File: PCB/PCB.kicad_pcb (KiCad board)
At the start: 4 copper layers, 54 x 29 mm, 90 parts, among them J1 USB_B_Micro, J2 Conn_01x02, Q1 PJA3428, Q2 PJA3428, Q3 AO3401A, SW1 SW_Push, SW2 SW_Push, SW3 SW_Push, SW4 ON/OFF, U1 ESP32-PICO-MINI-02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

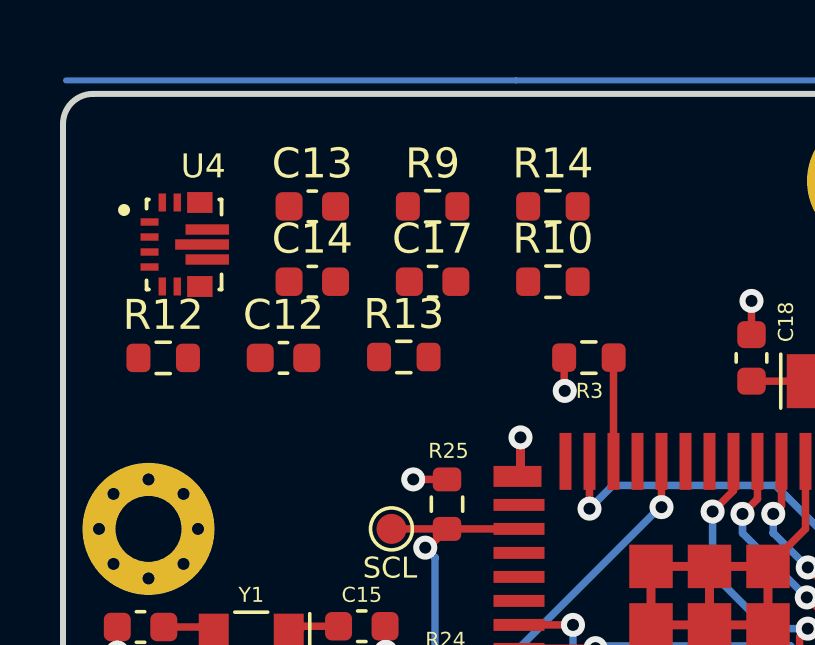
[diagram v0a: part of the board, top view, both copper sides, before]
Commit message: buck-boost pcb changes
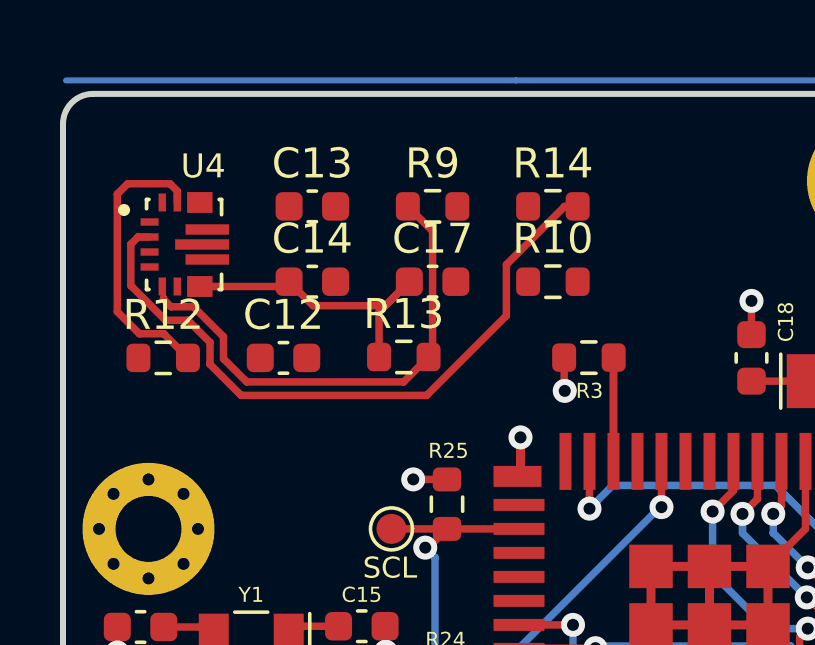
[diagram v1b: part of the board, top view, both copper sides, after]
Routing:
- net Net-(R14-Pad2): track 0.00 -> 22.5 mm
- net Net-(R13-Pad2): track 0.00 -> 16.2 mm
- net Net-(C14-Pad1): track 0.00 -> 10.6 mm
- net Net-(R10-Pad2): track 0.00 -> 9.54 mm
- net Net-(R3-Pad2): track 3.56 -> 7.02 mm
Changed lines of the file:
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@@
   (segment (start 235.85 95.61) (end 234.065 95.61) (width 0.25) (layer "B.Cu") (net 38))
   (segment (start 234.065 95.61) (end 232.575 97.1) (width 0.25) (layer "B.Cu") (net 38))
+  (segment (start 210.005 99.99) (end 210 99.995) (width 0.25) (layer "F.Cu") (net 39))
   (segment (start 210 99.995) (end 210 103.55) (width 0.25) (layer "F.Cu") (net 39))
-  (segment (start 210.005 99.99) (end 210 99.995) (width 0.25) (layer "F.Cu") (net 39))
+  (segment (start 210 99.995) (end 210 103.45) (width 0.25) (layer "F.Cu") (net 39))
   (segment (start 204.3175 113.6825) (end 204.425 113.575) (width 0.25) (layer "F.Cu") (net 40))
   (segment (start 201.5625 113.6825) (end 204.3175 113.6825) (width 0.25) (layer "F.Cu") (net 40))
@@
   (segment (start 238.5 101.275) (end 238.55 101.225) (width 0.25) (layer "B.Cu") (net 74))
   (segment (start 240.8 93.07) (end 243.055 93.07) (width 0.25) (layer "B.Cu") (net 74))
+  (segment (start 202.395 98.26) (end 203.195 97.46) (width 0.25) (layer "F.Cu") (net 75))
+  (segment (start 202.185 98.47) (end 202.185 99.97) (width 0.25) (layer "F.Cu") (net 75))
+  (segment (start 199.985 98.26) (end 202.395 98.26) (width 0.25) (layer "F.Cu") (net 75))
+  (segment (start 203.195 97.46) (end 202.185 98.47) (width 0.25) (layer "F.Cu") (net 75))
+  (segment (start 199.185 97.46) (end 199.985 98.26) (width 0.25) (layer "F.Cu") (net 75))
+  (segment (start 199.025 97.62) (end 199.185 97.46) (width 0.25) (layer "F.Cu") (net 75))
+  (segment (start 196.21 97.62) (end 199.025 97.62) (width 0.25) (layer "F.Cu") (net 75))
+  (segment (start 197.772183 100.8) (end 197 100.027817) (width 0.25) (layer "F.Cu") (net 76))
+  (segment (start 195.251845 98.295) (end 195 98.043155) (width 0.25) (layer "F.Cu") (net 76))
+  (segment (start 196 98.295) (end 195.251845 98.295) (width 0.25) (layer "F.Cu") (net 76))
+  (segment (start 203.835 99.97) (end 203.005 100.8) (width 0.25) (layer "F.Cu") (net 76))
+  (segment (start 197 99.295) (end 196 98.295) (width 0.25) (layer "F.Cu") (net 76))
+  (segment (start 203.005 100.8) (end 197.772183 100.8) (width 0.25) (layer "F.Cu") (net 76))
+  (segment (start 197 100.027817) (end 197 99.295) (width 0.25) (layer "F.Cu") (net 76))
+  (segment (start 203.97 99.835) (end 203.835 99.97) (width 0.25) (layer "F.Cu") (net 76))
+  (segment (start 195 98.043155) (end 195 98) (width 0.25) (layer "F.Cu") (net 76))
+  (segment (start 203.97 95.775) (end 203.97 99.835) (width 0.25) (layer "F.Cu") (net 76))
+  (segment (start 203.145 94.95) (end 203.97 95.775) (width 0.25) (layer "F.Cu") (net 76))
+  (segment (start 195.46 94.436845) (end 195.218155 94.195) (width 0.25) (layer "F.Cu") (net 77))
+  (segment (start 193.805 94.195) (end 193.46 94.54) (width 0.25) (layer "F.Cu") (net 77))
+  (segment (start 193.46 94.54) (end 193.46 98.46) (width 0.25) (layer "F.Cu") (net 77))
+  (segment (start 195.218155 94.195) (end 193.805 94.195) (width 0.25) (layer "F.Cu") (net 77))
+  (segment (start 195.46 94.82) (end 195.46 94.436845) (width 0.25) (layer "F.Cu") (net 77))
+  (segment (start 193.46 98.46) (end 194.195 99.195) (width 0.25) (layer "F.Cu") (net 77))
+  (segment (start 195.01 99.195) (end 195.815 100) (width 0.25) (layer "F.Cu") (net 77))
+  (segment (start 194.195 99.195) (end 195.01 99.195) (width 0.25) (layer "F.Cu") (net 77))
+  (segment (start 196.55 99.481396) (end 196.55 100.214213) (width 0.25) (layer "F.Cu") (net 78))
+  (segment (start 193.91 96.211845) (end 193.91 97.589551) (width 0.25) (layer "F.Cu") (net 78))
+  (segment (start 195.813604 98.745) (end 196.55 99.481396) (width 0.25) (layer "F.Cu") (net 78))
+  (segment (start 197.585787 101.25) (end 203.772462 101.25) (width 0.25) (layer "F.Cu") (net 78))
+  (segment (start 206.43 98.592462) (end 206.43 96.892462) (width 0.25) (layer "F.Cu") (net 78))
+  (segment (start 193.91 97.589551) (end 195.065449 98.745) (width 0.25) (layer "F.Cu") (net 78))
+  (segment (start 194.535 95.97) (end 194.151845 95.97) (width 0.25) (layer "F.Cu") (net 78))
+  (segment (start 203.772462 101.25) (end 206.43 98.592462) (width 0.25) (layer "F.Cu") (net 78))
+  (segment (start 194.151845 95.97) (end 193.91 96.211845) (width 0.25) (layer "F.Cu") (net 78))
+  (segment (start 195.065449 98.745) (end 195.813604 98.745) (width 0.25) (layer "F.Cu") (net 78))
+  (segment (start 196.55 100.214213) (end 197.585787 101.25) (width 0.25) (layer "F.Cu") (net 78))
+  (segment (start 208.372462 94.95) (end 208.805 94.95) (width 0.25) (layer "F.Cu") (net 78))
+  (segment (start 206.43 96.892462) (end 208.372462 94.95) (width 0.25) (layer "F.Cu") (net 78))
   (zone (net 30) (net_name "+3.3V") (layer "In1.Cu") (hatch edge 0.508)
     (connect_pads (clearance 0.508))

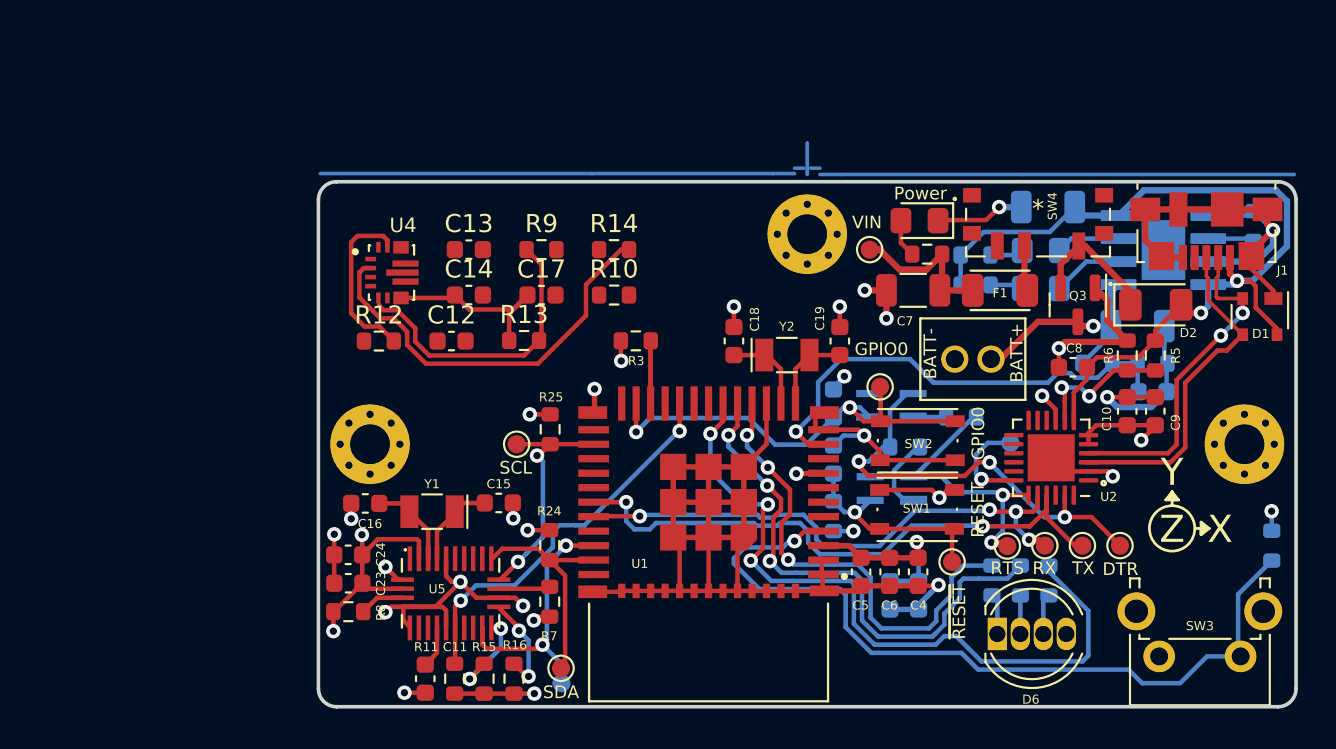
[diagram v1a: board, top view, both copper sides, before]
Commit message: huuuge rerouting and replacement. Added ESD protection resistors
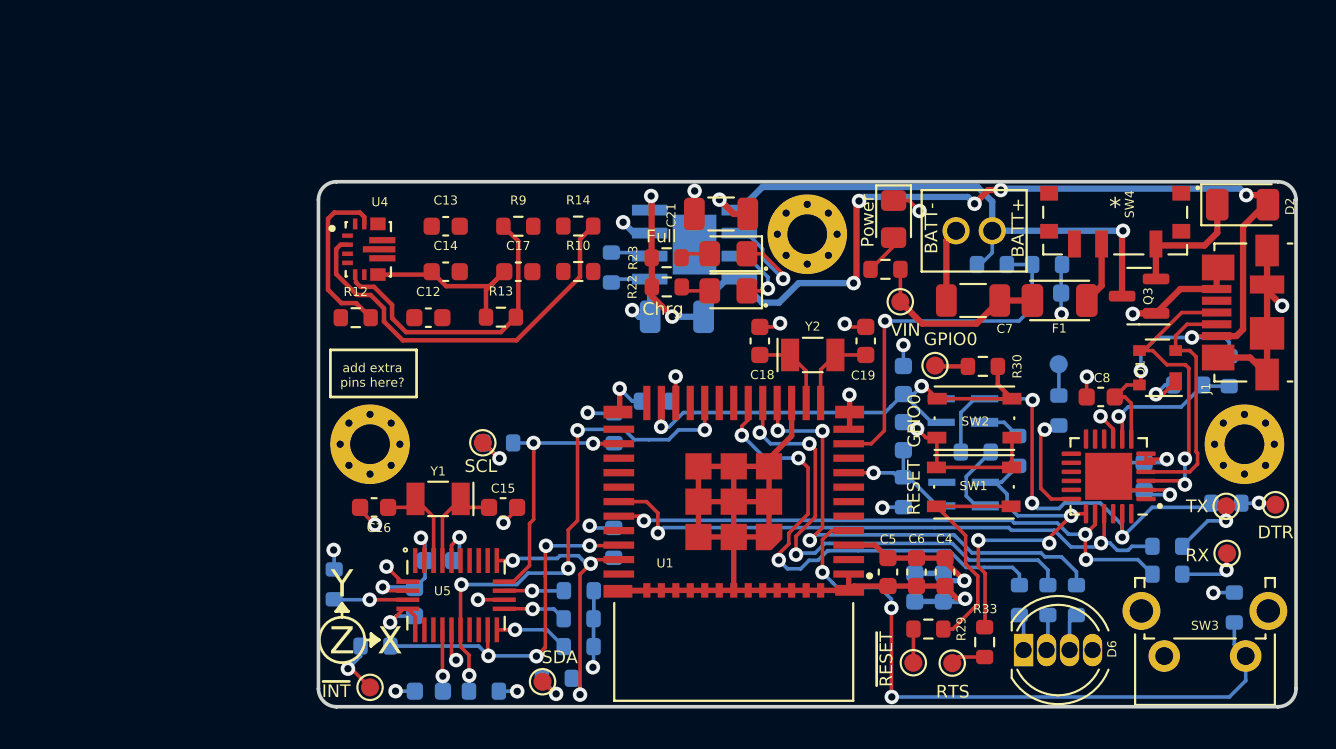
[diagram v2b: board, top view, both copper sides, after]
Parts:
- added R29: 22, Resistor_SMD:R_0603_1608Metric, F.Cu at (225.3, 115.9)
- added R30: 22, Resistor_SMD:R_0603_1608Metric, F.Cu at (228.3, 101.4)
- added R31: 22, Resistor_SMD:R_0603_1608Metric, B.Cu at (238.5, 111.3)
- added R32: 22, Resistor_SMD:R_0603_1608Metric, B.Cu at (238.5, 112.9)
- added R33: 22, Resistor_SMD:R_0603_1608Metric, F.Cu at (228.4, 116.6)
- added R34: 22, Resistor_SMD:R_0603_1608Metric, B.Cu at (232.6, 103.8)
- added R35: 22, Resistor_SMD:R_0603_1608Metric, B.Cu at (241.8, 109.0)
- added R36: 22, Resistor_SMD:R_0603_1608Metric, B.Cu at (204.8, 118.6)
- added R37: 22, Resistor_SMD:R_0603_1608Metric, B.Cu at (201.6, 105.6)
- added R38: 22, Resistor_SMD:R_0603_1608Metric, B.Cu at (194.8, 116.8)
- C10, C11, C23, C24, C9, R11, R15, R16, R24, R25, R3, R5, R6, R7, R8: moved to B.Cu
- C21, D7, D8, R22, R23, TP15: moved to F.Cu
- moved R20 35.5 mm to (207.8, 95.9), turned to 90 degrees
- moved U3 25.9 mm to (212.4, 94.7), turned to 0 degrees
- moved C21 23.8 mm to (213.9, 93.0), turned to 180 degrees
- moved C22 21.4 mm to (211.4, 98.7)
- moved D7 17.4 mm to (214.3, 97.2)
- moved D8 17.4 mm to (214.3, 95.2)
- moved R22 17.2 mm to (210.9, 97.0)
- moved R23 17.1 mm to (210.9, 95.4)
- moved TP15 10.6 mm to (194.5, 119.1), turned to -90 degrees
- moved TP5 10.1 mm to (241.8, 111.7)
- moved TP8 8.88 mm to (244.5, 109.0)
- moved TP4 8.23 mm to (241.8, 109.1)
- moved R26 7.98 mm to (228.8, 95.8)
- moved C25 7.98 mm to (231.9, 97.3)
- moved R27 7.98 mm to (231.9, 95.8)
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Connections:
- TP11 pad 1: ~{RESET} -> Net-(TP11-Pad1)
- TP12 pad 1: GPIO0 -> Net-(TP12-Pad1)
- TP13 pad 1: I2C_SDA -> Net-(TP13-Pad1)
- TP14 pad 1: I2C_SCL -> Net-(TP14-Pad1)
- TP15 pad 1: BNO_INTERRUPT -> Net-(TP15-Pad1)
- TP4 pad 1: PROG_TX -> Net-(TP4-Pad1)
- TP5 pad 1: PROG_RX -> Net-(TP5-Pad1)
- TP6 pad 1: PROG_RTS -> Net-(TP6-Pad1)
- TP7 pad 1: PROG_CTS -> Net-(TP7-Pad1)
- TP8 pad 1: PROG_DTR -> Net-(TP8-Pad1)
- U1 pad 15: RGB_RED -> RGB_BLUE
- U1 pad 17: RGB_BLUE -> RGB_RED
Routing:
- net GND: track 160.3 -> 135.5 mm, vias 23 -> 25
- net +5V: track 48.6 -> 71.6 mm, vias 2 -> 9
- net +BATT: track 12.8 -> 32.9 mm, vias 1 -> 2
- net RGB_BLUE: track 40.0 -> 26.8 mm
- net ~{BNO_RST}: track 21.5 -> 29.2 mm, vias 2 -> 5
- net SESSION_BUTTON: track 44.3 -> 36.7 mm, vias 1 -> 3
- net ~{RESET}: track 15.0 -> 20.4 mm, vias 2 -> 1
- net BATT_READ: track 25.9 -> 20.6 mm
- net +3.3V: track 40.8 -> 35.6 mm, vias 11 -> 12
- net BNO_INTERRUPT: track 15.4 -> 20.1 mm, vias 2 -> 4
- net USB_D-: track 18.5 -> 13.7 mm, vias 2 -> 0
- net PROG_RTS: track 15.4 -> 19.9 mm, vias 2 -> 3
- net Net-(TP4-Pad1): track 0.00 -> 3.80 mm, vias 0 -> 1
- net Net-(R3-Pad2): track 7.02 -> 3.33 mm, vias 0 -> 1
- net Net-(TP5-Pad1): track 0.00 -> 3.47 mm, vias 0 -> 1
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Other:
- board text added: "Chrg"
- board text added: "ECE477 Fall 2022 Brayden McNamara Ethan Crocker Kenzie Rappe Sean Boltjes"
- board text added: "Last Modified: 10/07/2022"
- board text added: "Team 13"
- board text added: "add extra pins here?"
- board text removed: "CTS"
- board text removed: "Charge"
- board text removed: "ECE477 Fall 2022 - Team 13 Brayden McNamara Ethan Crocker Kenzie Rappe Sean Boltjes"
- board text removed: "Last Modified: 10/03/2022"

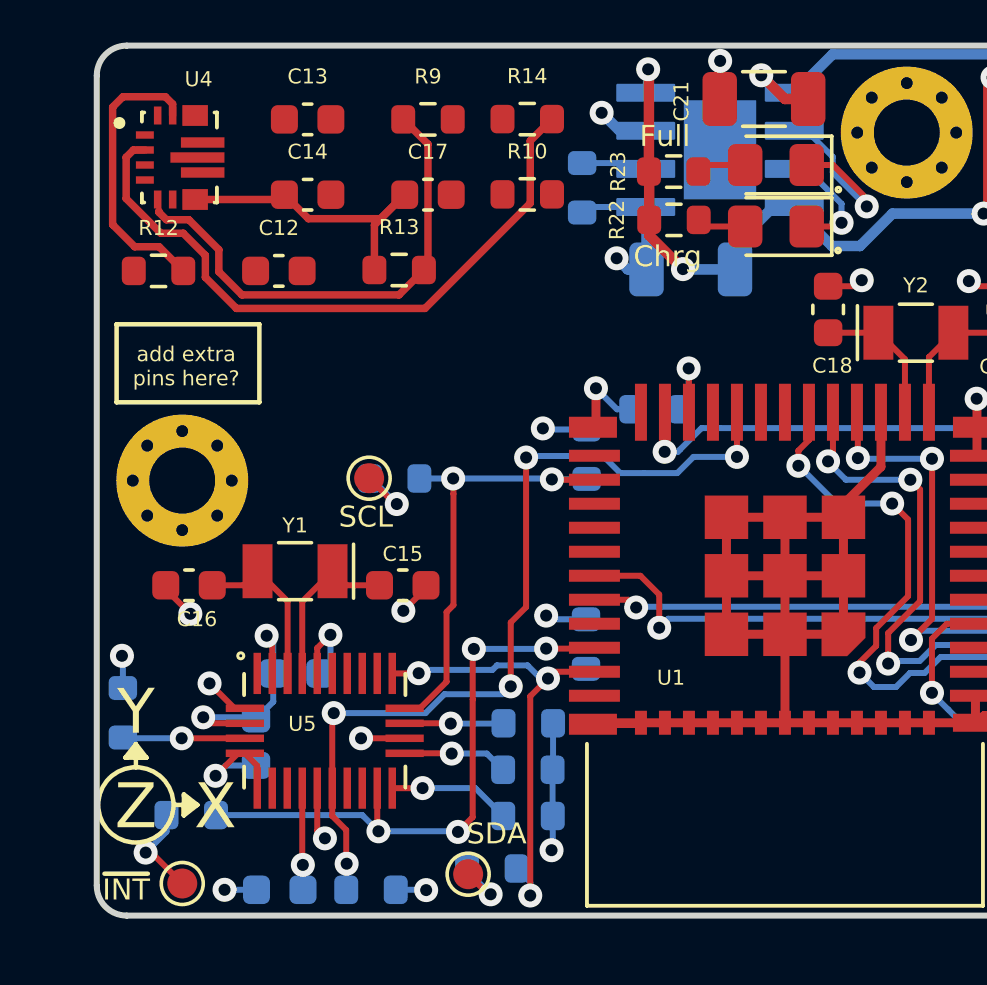
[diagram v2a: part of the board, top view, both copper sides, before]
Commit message: add JTAG support
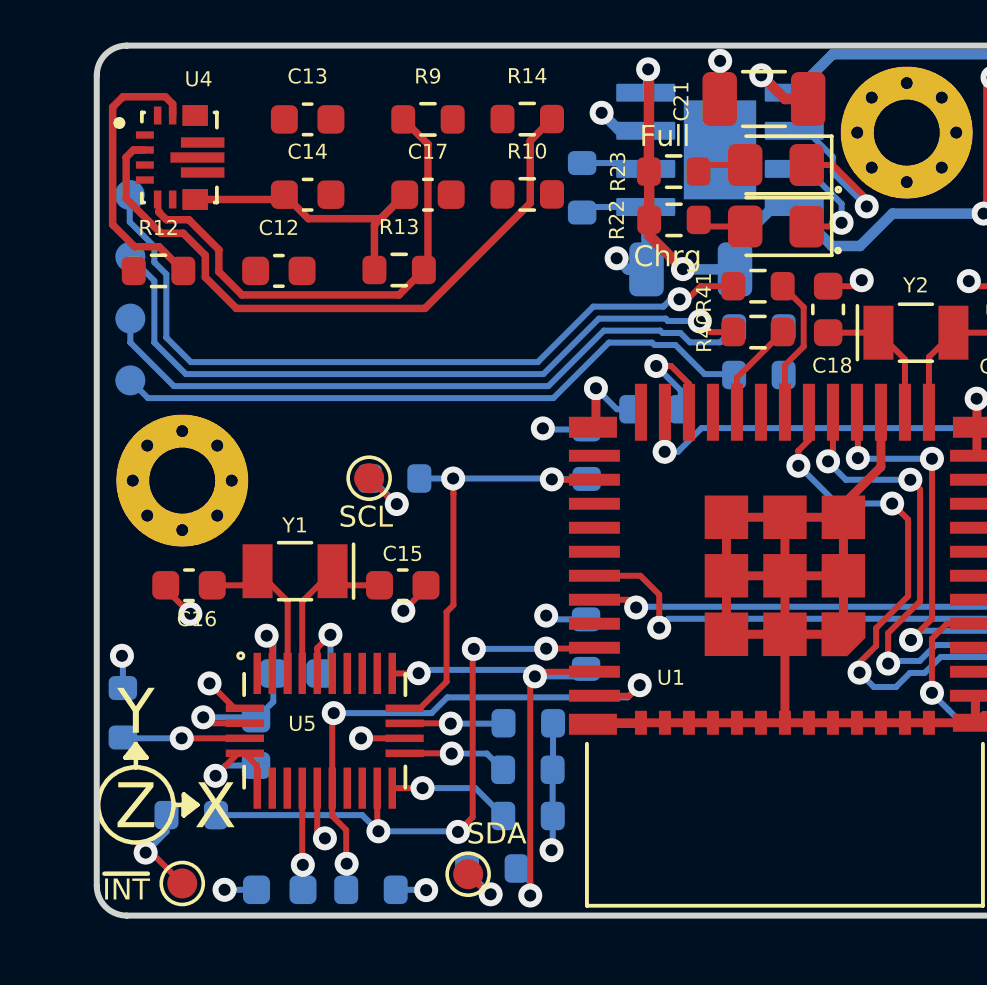
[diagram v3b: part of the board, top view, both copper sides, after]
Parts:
- added R39: 22, Resistor_SMD:R_0603_1608Metric, B.Cu at (213.7, 100.6)
- added R40: 22, Resistor_SMD:R_0603_1608Metric, F.Cu at (213.7, 100.8)
- added R41: 22, Resistor_SMD:R_0603_1608Metric, F.Cu at (213.7, 99.2)
- added R42: 22, Resistor_SMD:R_0603_1608Metric, B.Cu at (213.7, 102.2)
- added TP1: TDI, TestPoint:TestPoint_Pad_D1.0mm, B.Cu at (192.8, 100.3)
- added TP10: TDO, TestPoint:TestPoint_Pad_D1.0mm, B.Cu at (192.8, 102.4)
- added TP2: TCK, TestPoint:TestPoint_Pad_D1.0mm, B.Cu at (192.8, 98.2)
- added TP9: TMS, TestPoint:TestPoint_Pad_D1.0mm, B.Cu at (192.8, 96.2)
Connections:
- U1 pad 18: unconnected-(U1-Pad18) -> JTAG_TMS
- U1 pad 19: unconnected-(U1-Pad19) -> JTAG_TDI
- U1 pad 20: ~{BNO_RST} -> JTAG_TCK
- U1 pad 21: unconnected-(U1-Pad21) -> JTAG_TDO
- U1 pad 35: unconnected-(U1-Pad35) -> ~{BNO_RST}
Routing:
- net Net-(R41-Pad1): track 0.00 -> 25.5 mm, vias 0 -> 1
- net Net-(R40-Pad1): track 0.00 -> 23.9 mm, vias 0 -> 1
- net Net-(R39-Pad1): track 0.00 -> 22.6 mm
- net Net-(R42-Pad1): track 0.00 -> 21.6 mm
- net ~{BNO_RST}: track 29.2 -> 18.4 mm, vias 5 -> 3
- net JTAG_TMS: track 0.00 -> 4.75 mm
- net JTAG_TCK: track 0.00 -> 3.30 mm
- net I2C_SDA: track 15.7 -> 17.2 mm
- net Net-(R3-Pad2): track 3.33 -> 4.07 mm
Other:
- board text added: "CTS"
- board text added: "JTAG"
- board text added: "TCK"
- board text added: "TDI"
- board text added: "TDO"
- board text added: "TMS"
- board text removed: "add extra pins here?"
